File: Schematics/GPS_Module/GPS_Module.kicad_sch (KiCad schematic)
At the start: 70 parts, among them J1 GT8E-6P-2H(55), J2 SWD_01x04_Pin, J4 Stack Male Edge Connector, J4 USB_C_Female_USB2_Small, SW1 SW_STM_RESET, SW2 SW_STM_BOOT_MODE, U1 CP2102N-Axx-xQFN28, U1 STM32F103CBT6, U10 TPM8837C-SO1R, U12 AMS1117-3.3, U2 W25Q128JVS, U4 LM66100DCKR, U5 LM66100DCKR, U6 LM66100DCKR, U9 ISO1042BQDWVR, Y1 X322516MMB4SI

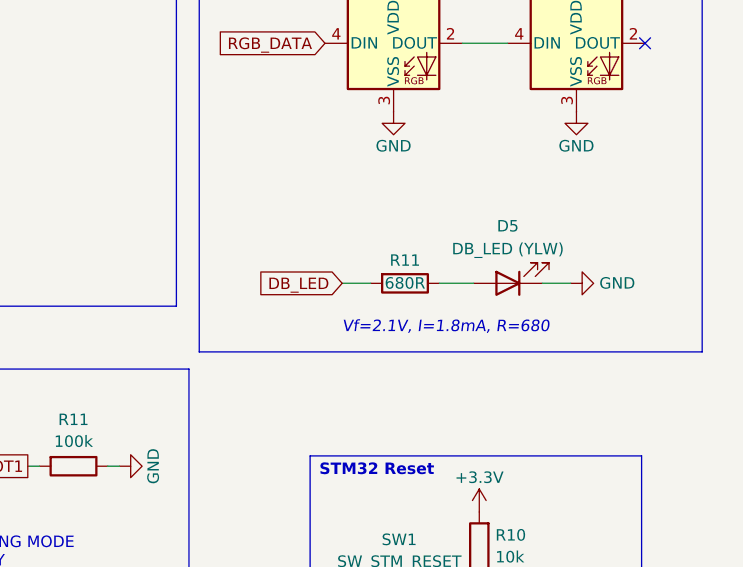
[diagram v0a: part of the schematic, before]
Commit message: prepare for dedicated av-recovery repo (GPS & Altimter only)
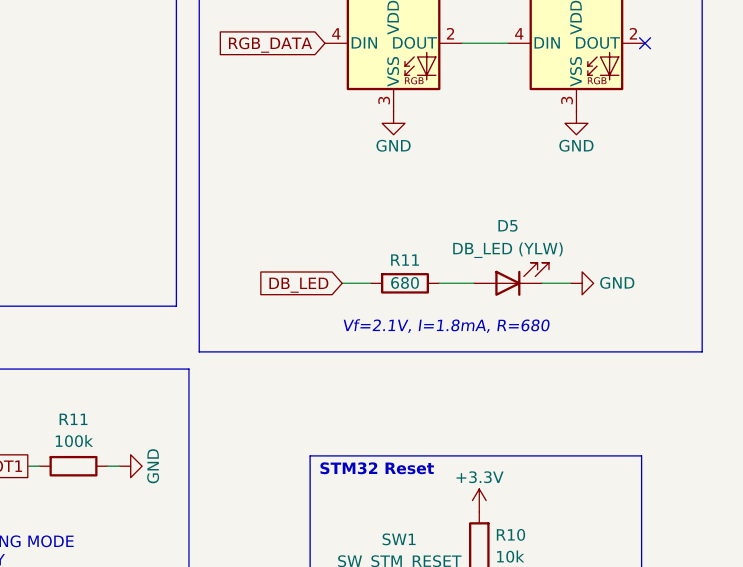
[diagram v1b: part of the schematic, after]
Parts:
- C1, C3: JLCPCB C96446 -> (none); LCSC (none) -> C96446
- C10, C12, C13, C9: JLCPCB C1525 -> (none); LCSC (none) -> C1525
- C14: JLCPCB C57112 -> (none); LCSC (none) -> C57112
- C16, C18: JLCPCB C1634 -> (none); LCSC (none) -> C1634
- C18, C2, C? (x3): JLCPCB C14663 -> (none); LCSC (none) -> C14663
- C20, C21: JLCPCB C28323 -> (none); LCSC (none) -> C28323
- C3, C4, C5, C6: JLCPCB C15849 -> (none); LCSC (none) -> C15849
- D1: JLCPCB C2297 -> (none); LCSC (none) -> C2297
- D5, D6: JLCPCB C191023 -> (none); LCSC (none) -> C191023
- D5: JLCPCB C72038 -> (none); LCSC (none) -> C72038
- FB1: JLCPCB C1015 -> (none); LCSC (none) -> C1015
- J4: JLCPCB C5178541 -> (none); LCSC (none) -> C5178541
- R1, R10, R3: JLCPCB C25804 -> (none); LCSC (none) -> C25804
- R11, R6: JLCPCB C25803 -> (none); LCSC (none) -> C25803
- R11: value 680R -> 680; JLCPCB C23228 -> (none); LCSC (none) -> C23228
- R28, R29: JLCPCB C23186 -> (none); LCSC (none) -> C23186
- R29: JLCPCB C21190 -> (none); LCSC (none) -> C21190
- R30: JLCPCB C31850 -> (none); LCSC (none) -> C31850
- R31: JLCPCB C25819 -> (none); LCSC (none) -> C25819
- R5, R6: JLCPCB C4190 -> (none); LCSC (none) -> C4190
- R5: JLCPCB C22978 -> (none); LCSC (none) -> C22978
- R8: JLCPCB C22843 -> (none); LCSC (none) -> C22843
- SW1, SW2: JLCPCB C318884 -> (none); LCSC (none) -> C318884
- U1: JLCPCB C8304 -> (none); LCSC (none) -> C8304
- U1: JLCPCB C6568 -> (none); LCSC (none) -> C6568
- U12: JLCPCB C6186 -> (none); LCSC (none) -> C6186
- U2: JLCPCB C97521 -> (none); LCSC (none) -> C97521
- U4, U5, U6: JLCPCB C2869734 -> (none); LCSC (none) -> C2869734
- U9: JLCPCB C484409 -> (none); LCSC (none) -> C484409
- Y1: JLCPCB C13738 -> (none); LCSC (none) -> C13738
